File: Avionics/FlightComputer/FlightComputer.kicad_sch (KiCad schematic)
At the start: 35 parts

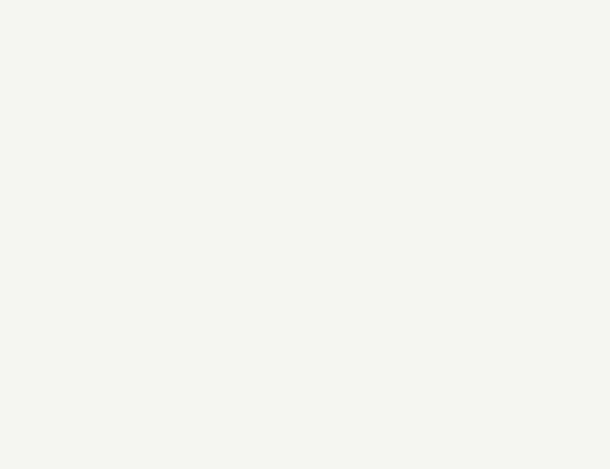
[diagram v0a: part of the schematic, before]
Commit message: IanGoldberg; Added another sheet to the flight computer design containing (some) of the pins for the Texas Instruments SubArctic AM335x processor. Checked with others, all pins so far seem correct.
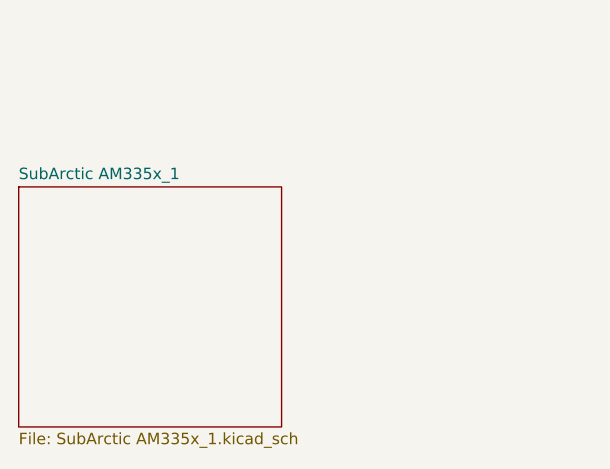
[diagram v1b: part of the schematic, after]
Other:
- added sheet SubArctic AM335x_1 (SubArctic AM335x_1.kicad_sch)
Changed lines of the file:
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@@
+		)
+	)
+	(sheet
+		(at 34.29 143.51)
+		(size 29.21 26.67)
+		(fields_autoplaced yes)
+		(stroke
+			(width 0.1524)
+			(type solid)
+		)
+		(fill
+			(color 0 0 0 0.0000)
+		)
+		(property "Sheetname" "SubArctic AM335x_1"
+			(at 34.29 142.7984 0)
+			(effects
+				(font
+					(size 1.27 1.27)
+				)
+				(justify left bottom)
+			)
+		)
+		(property "Sheetfile" "SubArctic AM335x_1.kicad_sch"
+			(at 34.29 170.7646 0)
+			(effects
+				(font
+					(size 1.27 1.27)
+				)
+				(justify left top)
+			)
+		)
+		(instances
+			(project "FlightComputer"
+				(path "/80fd70cc-258e-4c36-a149-cd51380d23dc"
+					(page "2")
+				)
+			)
 		)
 	)

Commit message: Ian Goldberg - Made substantial additions to the main chip of the flight computer. Wrapping up progress for the night.
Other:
- added sheet SubArcticSheet2 (Subarcticsheet2.kicad_sch)
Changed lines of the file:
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@@
+		)
+	)
+	(sheet
+		(at 71.12 139.7)
+		(size 29.21 27.94)
+		(fields_autoplaced yes)
+		(stroke
+			(width 0.1524)
+			(type solid)
+		)
+		(fill
+			(color 0 0 0 0.0000)
+		)
+		(property "Sheetname" "SubArcticSheet2"
+			(at 71.12 138.9884 0)
+			(effects
+				(font
+					(size 1.27 1.27)
+				)
+				(justify left bottom)
+			)
+		)
+		(property "Sheetfile" "Subarcticsheet2.kicad_sch"
+			(at 71.12 168.2246 0)
+			(effects
+				(font
+					(size 1.27 1.27)
+				)
+				(justify left top)
+			)
+		)
+		(property "Field2" ""
+			(at 71.12 139.7 0)
+			(effects
+				(font
+					(size 1.27 1.27)
+				)
+				(hide yes)
+			)
+		)
+		(instances
+			(project "FlightComputer"
+				(path "/80fd70cc-258e-4c36-a149-cd51380d23dc"
+					(page "3")
+				)
+			)
 		)
 	)

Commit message: Ian Goldberg - Made changes to the Flight Computer sheet
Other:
- sheet SubArcticSheet2 renamed SubArctic AM335x_2
- sheet SubArctic AM335x_2: file Subarcticsheet2.kicad_sch -> SubArctic AM335x_2.kicad_sch
- note added: "6.15.24"
- note added: "Flight computer "Erebus" - V1.1 - Ian Goldberg"
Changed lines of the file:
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@@
 		)
 	)
+	(text "Flight computer \"Erebus\" - V1.1 - Ian Goldberg\n\n"
+		(exclude_from_sim no)
+		(at 216.408 191.008 0)
+		(effects
+			(font
+				(size 1.524 1.524)
+				(thickness 0.254)
+				(bold yes)
+			)
+		)
+	)
+	(text "6.15.24\n"
+		(exclude_from_sim no)
+		(at 210.312 193.548 0)
+		(effects
+			(font
+				(size 1.27 1.27)
+			)
+		)
+	)
 	(global_label "PWR_BUT"
 		(shape input)
@@
 	)
 	(sheet
-		(at 34.29 143.51)
-		(size 29.21 26.67)
+		(at 19.05 144.78)
+		(size 33.02 19.05)
 		(fields_autoplaced yes)
 		(stroke
@@
 		)
 		(property "Sheetname" "SubArctic AM335x_1"
-			(at 34.29 142.7984 0)
+			(at 19.05 144.0684 0)
 			(effects
 				(font
@@
 		)
 		(property "Sheetfile" "SubArctic AM335x_1.kicad_sch"
-			(at 34.29 170.7646 0)
+			(at 19.05 164.4146 0)
 			(effects
 				(font
@@
 	)
 	(sheet
-		(at 71.12 139.7)
-		(size 29.21 27.94)
+		(at 55.88 144.78)
+		(size 31.75 19.05)
 		(fields_autoplaced yes)
 		(stroke
@@
 			(color 0 0 0 0.0000)
 		)
-		(property "Sheetname" "SubArcticSheet2"
-			(at 71.12 138.9884 0)
+		(property "Sheetname" "SubArctic AM335x_2"
+			(at 55.88 144.0684 0)
 			(effects
 				(font
@@
 			)
 		)
-		(property "Sheetfile" "Subarcticsheet2.kicad_sch"
-			(at 71.12 168.2246 0)
+		(property "Sheetfile" "SubArctic AM335x_2.kicad_sch"
+			(at 55.88 164.4146 0)
 			(effects
 				(font
@@
 		)
 		(property "Field2" ""
-			(at 71.12 139.7 0)
+			(at 55.88 144.78 0)
 			(effects
 				(font

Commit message: Ian Goldberg - made final changes to the flight computer schematic
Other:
- note added: "Flight computer "Erebos" - V1.1 - Ian Goldberg"
- note removed: "Flight computer "Erebus" - V1.1 - Ian Goldberg"
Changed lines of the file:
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@@
 		)
 	)
-	(text "Flight computer \"Erebus\" - V1.1 - Ian Goldberg\n\n"
+	(text "Flight computer \"Erebos\" - V1.1 - Ian Goldberg\n\n"
 		(exclude_from_sim no)
 		(at 216.408 191.008 0)

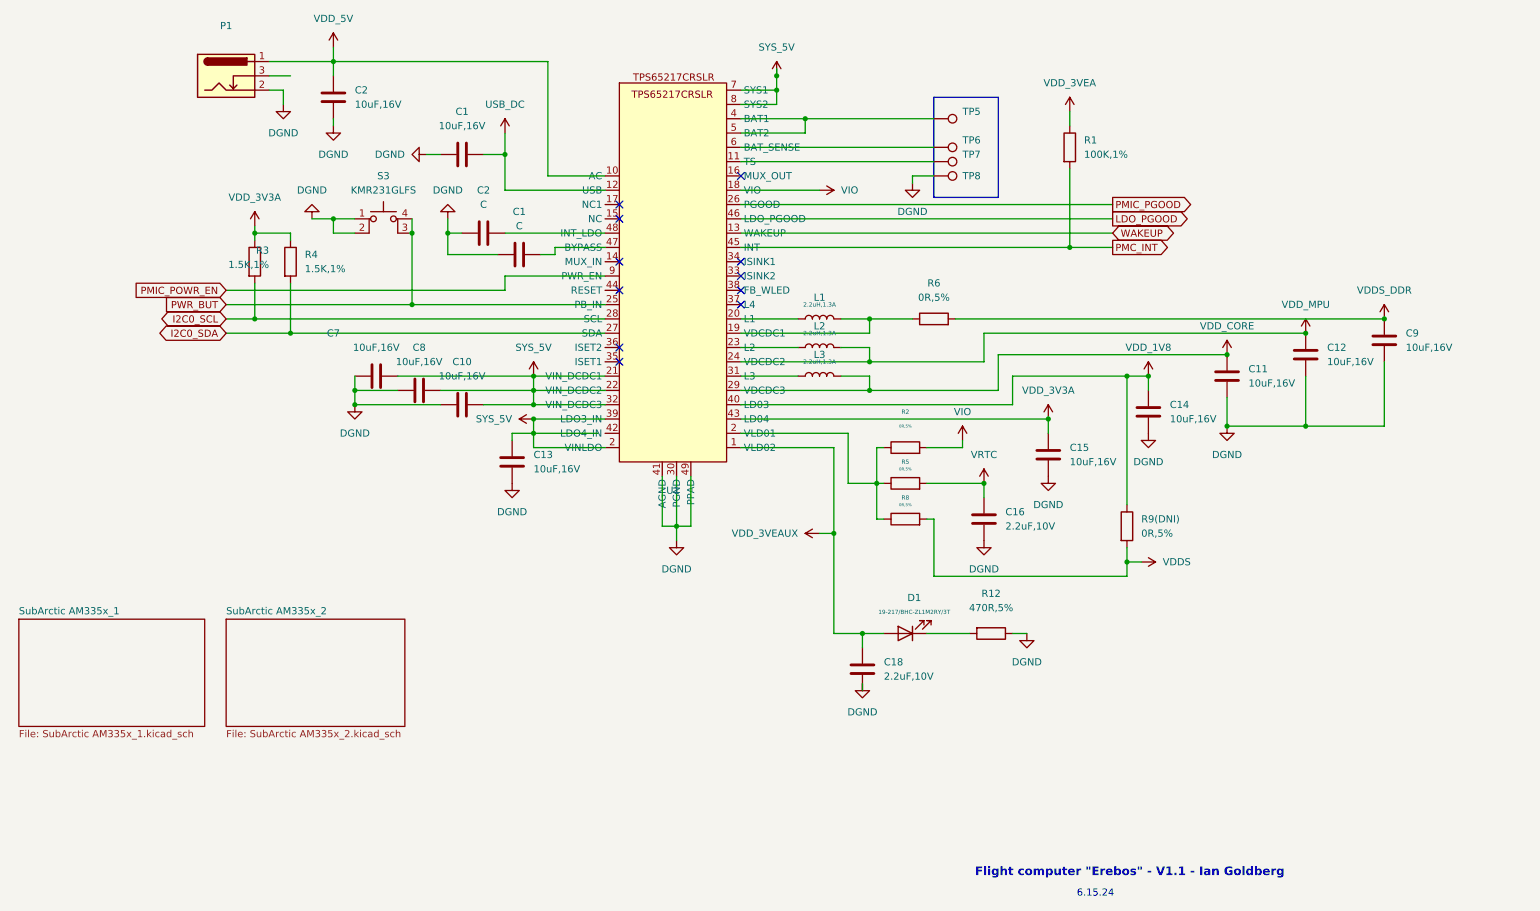
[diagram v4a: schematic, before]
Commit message: Ian Goldberg - Finished the second pin diagram for the SubArctic AM335x chip - only one more to go after this one.
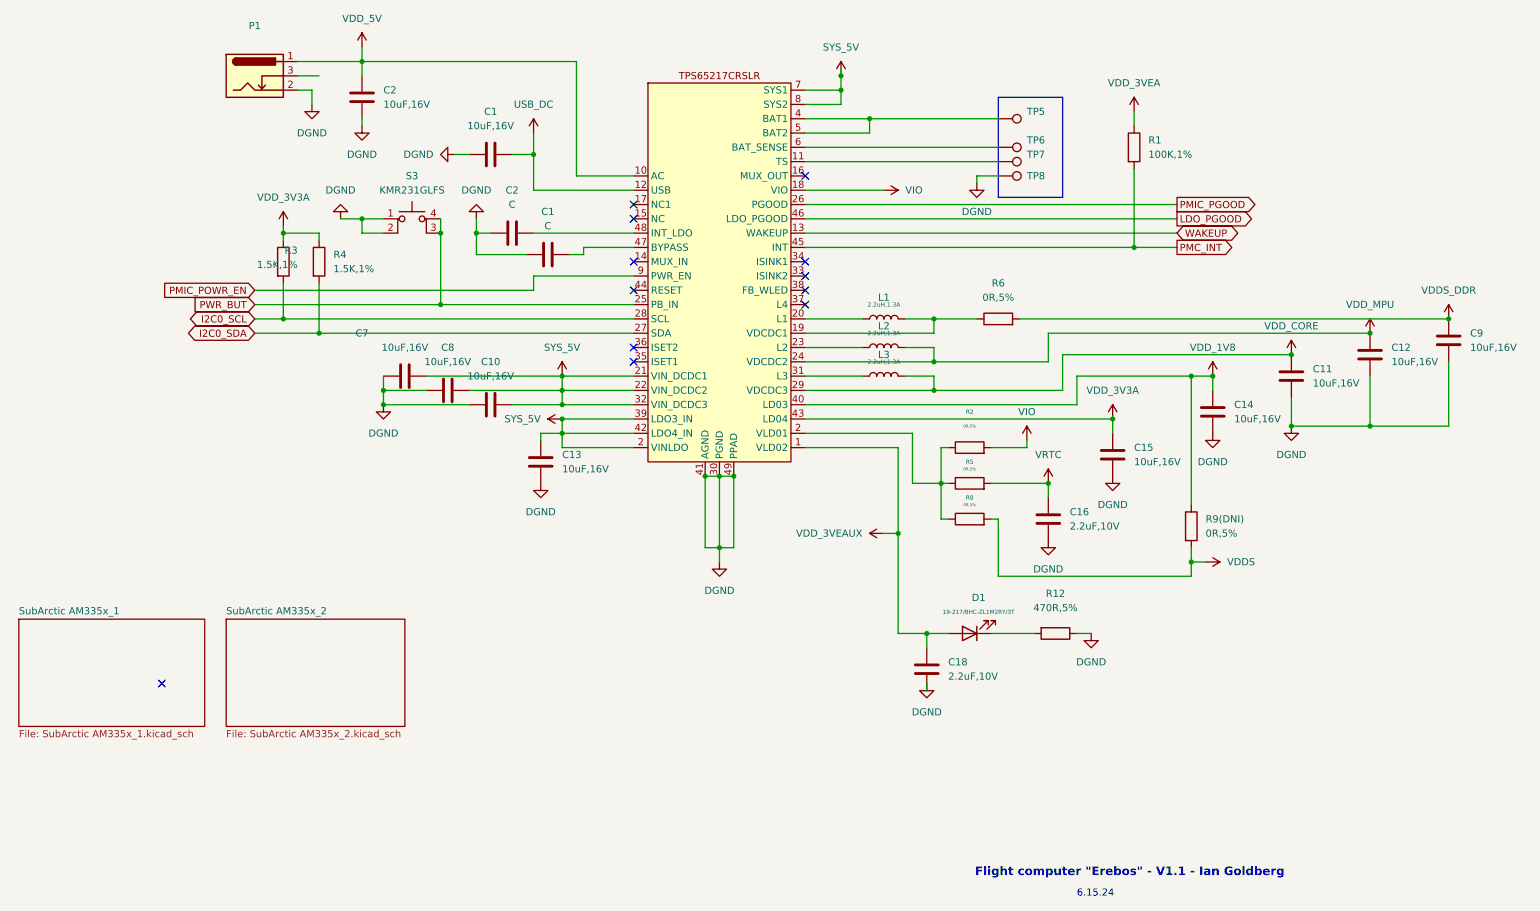
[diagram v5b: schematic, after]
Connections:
- net DGND: now also U1.30 (PGND), U1.41 (AGND), U1.49 (PPAD)
- net I2C0_SCL: now also U1.28 (SCL)
- net I2C0_SDA: now also U1.27 (SDA)
- net LDO_PGOOD: now also U1.46 (LDO_PGOOD)
- net PMC_INT: now also U1.45 (INT)
- net PMIC_PGOOD : now also U1.26 (PGOOD)
- net PMIC_POWR_EN: now also U1.9 (PWR_EN)
- net PWR_BUT: now also U1.25 (PB_IN)
- net SYS_5V: now also U1.2 (VLD01), U1.21 (VIN_DCDC1), U1.22 (VIN_DCDC2), U1.32 (VIN_DCDC3), U1.39 (LDO3_IN), U1.42 (LDO4_IN), U1.7 (SYS1), U1.8 (SYS2)
- net USB_DC: now also U1.12 (USB)
- net VDD_1V8: now also U1.40 (LD03)
- net VDD_3V3A: now also U1.43 (LD04)
- net VDD_3VEAUX: now also U1.1 (VLD02)
- net VDD_5V: now also U1.10 (AC)
- net VDD_CORE: now also U1.29 (VDCDC3)
- net VDD_MPU: now also U1.24 (VDCDC2)
- net VIO: now also U1.18 (VIO)
- net WAKEUP: now also U1.13 (WAKEUP)
- net at R2.1, R5.1, R8.1: now also U1.2 (VLD01)
- net at TP5.1: now also U1.4 (BAT1), U1.5 (BAT2)
- net at U1.11 (TS): now also TP7.1
- net at U1.19 (VDCDC1): now also L1.2, R6.1
- net at U1.20 (L1): now also L1.1
- net at U1.23 (L2): now also L2.1
- net at U1.31 (L3): now also L3.1
- net at U1.47 (BYPASS): now also C1.2
- net at U1.48 (INT_LDO): now also C2.2
- net at U1.6 (BAT_SENSE): now also TP6.1
- no-connect marks 11 -> 12
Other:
- moved on the sheet: C1, C10, C11, C12, C13, C14, C15, C16, C18, C2, C7, C8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

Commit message: Ian Goldberg - Finished the pin-out for the third schematic of the SubArctic chip. All that remains is finishing up the rest of the circuit.
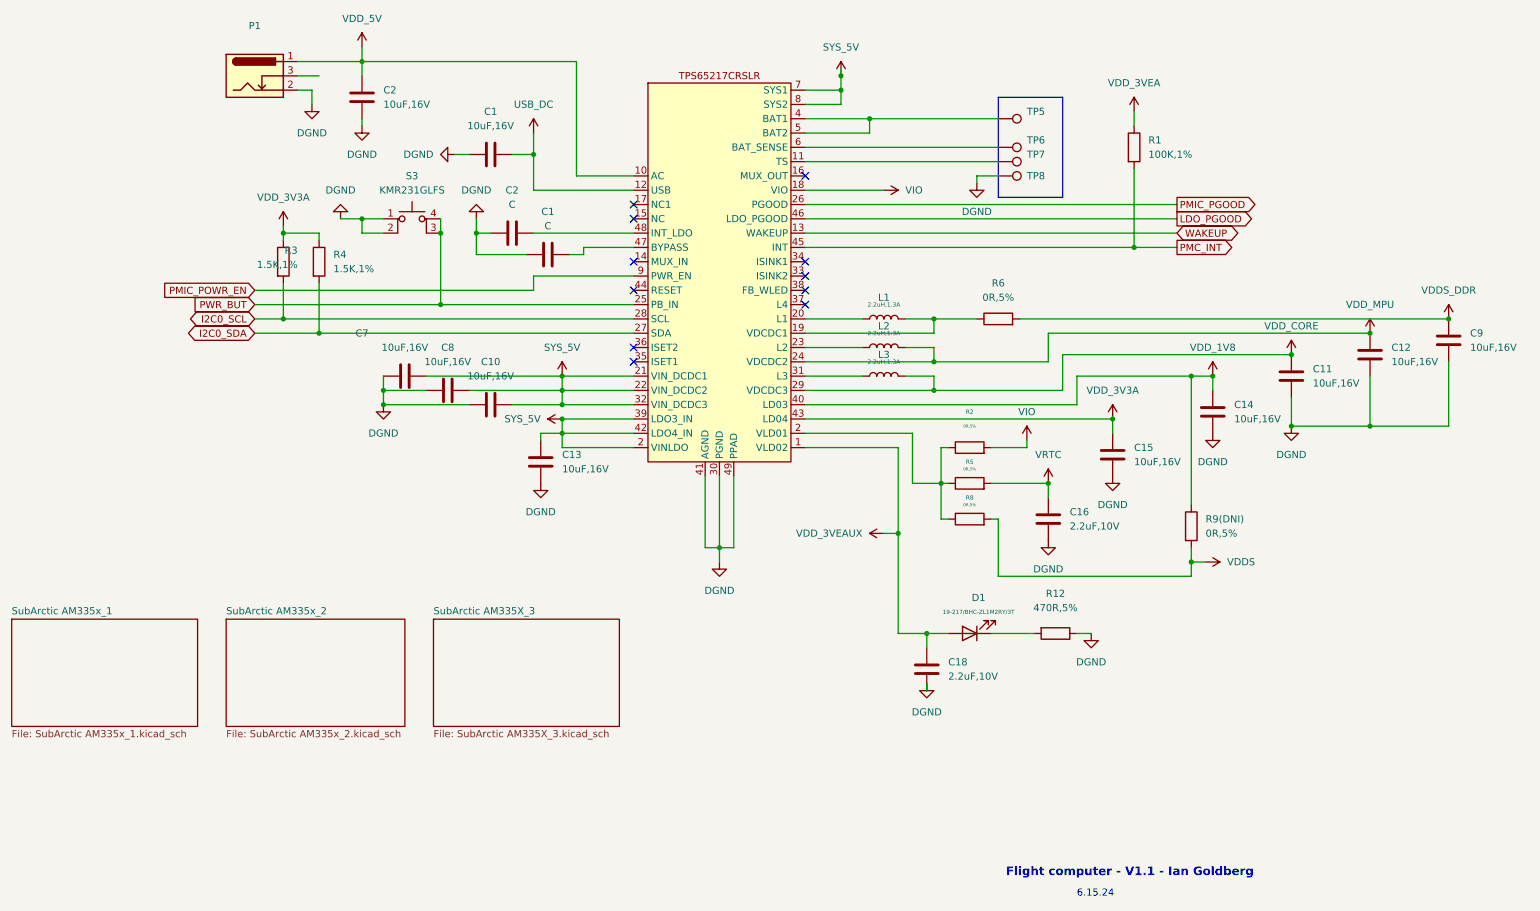
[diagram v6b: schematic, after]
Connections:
- no-connect marks 12 -> 11
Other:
- added sheet SubArctic AM335X_3 (SubArctic AM335X_3.kicad_sch)
- note added: "Flight computer - V1.1 - Ian Goldberg"
- note removed: "Flight computer "Erebos" - V1.1 - Ian Goldberg"
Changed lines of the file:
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@@
 	)
 	(junction
-		(at 143.51 119.38)
-		(diameter 0)
-		(color 0 0 0 0)
-	)
-	(junction
 		(at 213.36 109.22)
 		(diameter 0)
@@
 	)
 	(junction
-		(at 140.97 119.38)
-		(diameter 0)
-		(color 0 0 0 0)
-	)
-	(junction
 		(at 83.82 104.14)
 		(diameter 0)
@@
 	)
 	(junction
-		(at 146.05 119.38)
-		(diameter 0)
-		(color 0 0 0 0)
-	)
-	(junction
 		(at 115.57 104.14)
 		(diameter 0)
@@
 	)
 	(no_connect
-		(at 44.45 156.21)
-	)
-	(no_connect
 		(at 128.27 81.28)
 	)
@@
 	(wire
 		(pts
-			(xy 146.05 119.38) (xy 143.51 119.38)
-		)
-		(stroke
-			(width 0)
-			(type default)
-		)
-	)
-	(wire
-		(pts
 			(xy 175.26 129.54) (xy 175.26 147.32)
 		)
@@
 	(wire
 		(pts
-			(xy 143.51 119.38) (xy 140.97 119.38)
-		)
-		(stroke
-			(width 0)
-			(type default)
-		)
-	)
-	(wire
-		(pts
 			(xy 193.04 137.16) (xy 227.33 137.16)
 		)
@@
 		)
 	)
-	(text "Flight computer \"Erebos\" - V1.1 - Ian Goldberg\n\n"
+	(text "Flight computer - V1.1 - Ian Goldberg\n\n"
 		(exclude_from_sim no)
 		(at 216.408 191.008 0)
@@
 	)
 	(sheet
-		(at 19.05 144.78)
+		(at 92.71 144.78)
+		(size 33.02 19.05)
+		(fields_autoplaced yes)
+		(stroke
+			(width 0.1524)
+			(type solid)
+		)
+		(fill
+			(color 0 0 0 0.0000)
+		)
+		(property "Sheetname" "SubArctic AM335X_3"
+			(at 92.71 144.0684 0)
+			(effects
+				(font
+					(size 1.27 1.27)
+				)
+				(justify left bottom)
+			)
+		)
+		(property "Sheetfile" "SubArctic AM335X_3.kicad_sch"
+			(at 92.71 164.4146 0)
+			(effects
+				(font
+					(size 1.27 1.27)
+				)
+				(justify left top)
+			)
+		)
+		(instances
+			(project "FlightComputer"
+				(path "/80fd70cc-258e-4c36-a149-cd51380d23dc"
+					(page "4")
+				)
+			)
+		)
+	)
+	(sheet
+		(at 17.78 144.78)
 		(size 33.02 19.05)
 		(fields_autoplaced yes)
@@
 		)
 		(property "Sheetname" "SubArctic AM335x_1"
-			(at 19.05 144.0684 0)
+			(at 17.78 144.0684 0)
 			(effects
 				(font
@@
 		)
 		(property "Sheetfile" "SubArctic AM335x_1.kicad_sch"
-			(at 19.05 164.4146 0)
+			(at 17.78 164.4146 0)
 			(effects
 				(font

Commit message: Ian Goldberg - Added the 4th sheet to the flight computer schematic{
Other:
- added sheet Sheet 4 (Flightcomputersheet4.kicad_sch)
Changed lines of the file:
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@@
+	)
+	(sheet
+		(at 17.78 168.91)
+		(size 33.02 20.32)
+		(fields_autoplaced yes)
+		(stroke
+			(width 0.1524)
+			(type solid)
+		)
+		(fill
+			(color 0 0 0 0.0000)
+		)
+		(property "Sheetname" "Sheet 4"
+			(at 17.78 168.1984 0)
+			(effects
+				(font
+					(size 1.27 1.27)
+				)
+				(justify left bottom)
+			)
+		)
+		(property "Sheetfile" "Flightcomputersheet4.kicad_sch"
+			(at 17.78 189.8146 0)
+			(effects
+				(font
+					(size 1.27 1.27)
+				)
+				(justify left top)
+			)
+		)
+		(instances
+			(project "FlightComputer"
+				(path "/80fd70cc-258e-4c36-a149-cd51380d23dc"
+					(page "5")
+				)
+			)
+		)
 	)
 	(sheet

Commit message: Ian Goldberg - Making updates to the design for the flight computer
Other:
- added sheet Sheet 5 (Flightcomputersheet5.kicad_sch)
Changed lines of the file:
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@@
+	)
+	(sheet
+		(at 55.88 168.91)
+		(size 31.75 20.32)
+		(fields_autoplaced yes)
+		(stroke
+			(width 0.1524)
+			(type solid)
+		)
+		(fill
+			(color 0 0 0 0.0000)
+		)
+		(property "Sheetname" "Sheet 5"
+			(at 55.88 168.1984 0)
+			(effects
+				(font
+					(size 1.27 1.27)
+				)
+				(justify left bottom)
+			)
+		)
+		(property "Sheetfile" "Flightcomputersheet5.kicad_sch"
+			(at 55.88 189.8146 0)
+			(effects
+				(font
+					(size 1.27 1.27)
+				)
+				(justify left top)
+			)
+		)
+		(property "Field2" ""
+			(at 55.88 168.91 0)
+			(effects
+				(font
+					(size 1.27 1.27)
+				)
+				(hide yes)
+			)
+		)
+		(instances
+			(project "FlightComputer"
+				(path "/80fd70cc-258e-4c36-a149-cd51380d23dc"
+					(page "6")
+				)
+			)
+		)
 	)
 	(sheet
